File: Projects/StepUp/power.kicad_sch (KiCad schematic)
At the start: 28 parts, among them J2 USB_B_Micro, U2 NCP1117-3.3_SOT223, U3 MIC2253, U7 MCP73832T-2ACI_OT, U8 USBLC6-2SC6

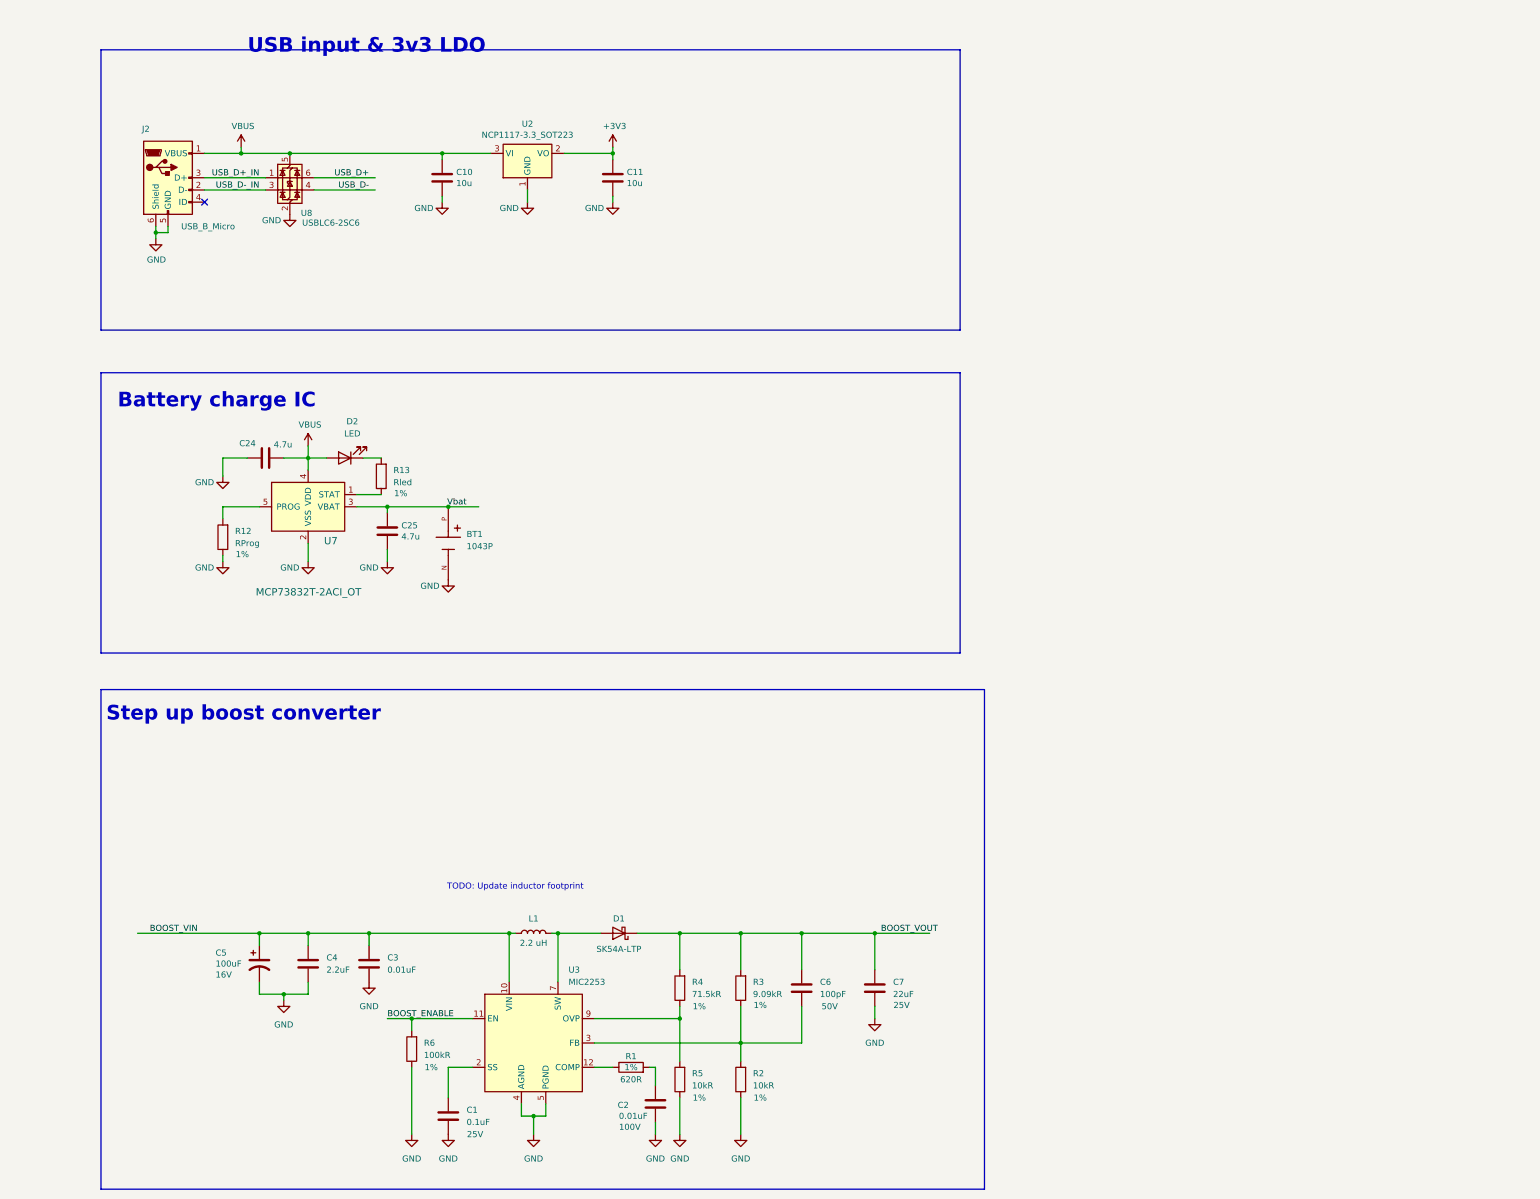
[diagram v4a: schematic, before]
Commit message: feat(power): Input stage updates
USB vs Vbat source selection using PMOS gate logic.
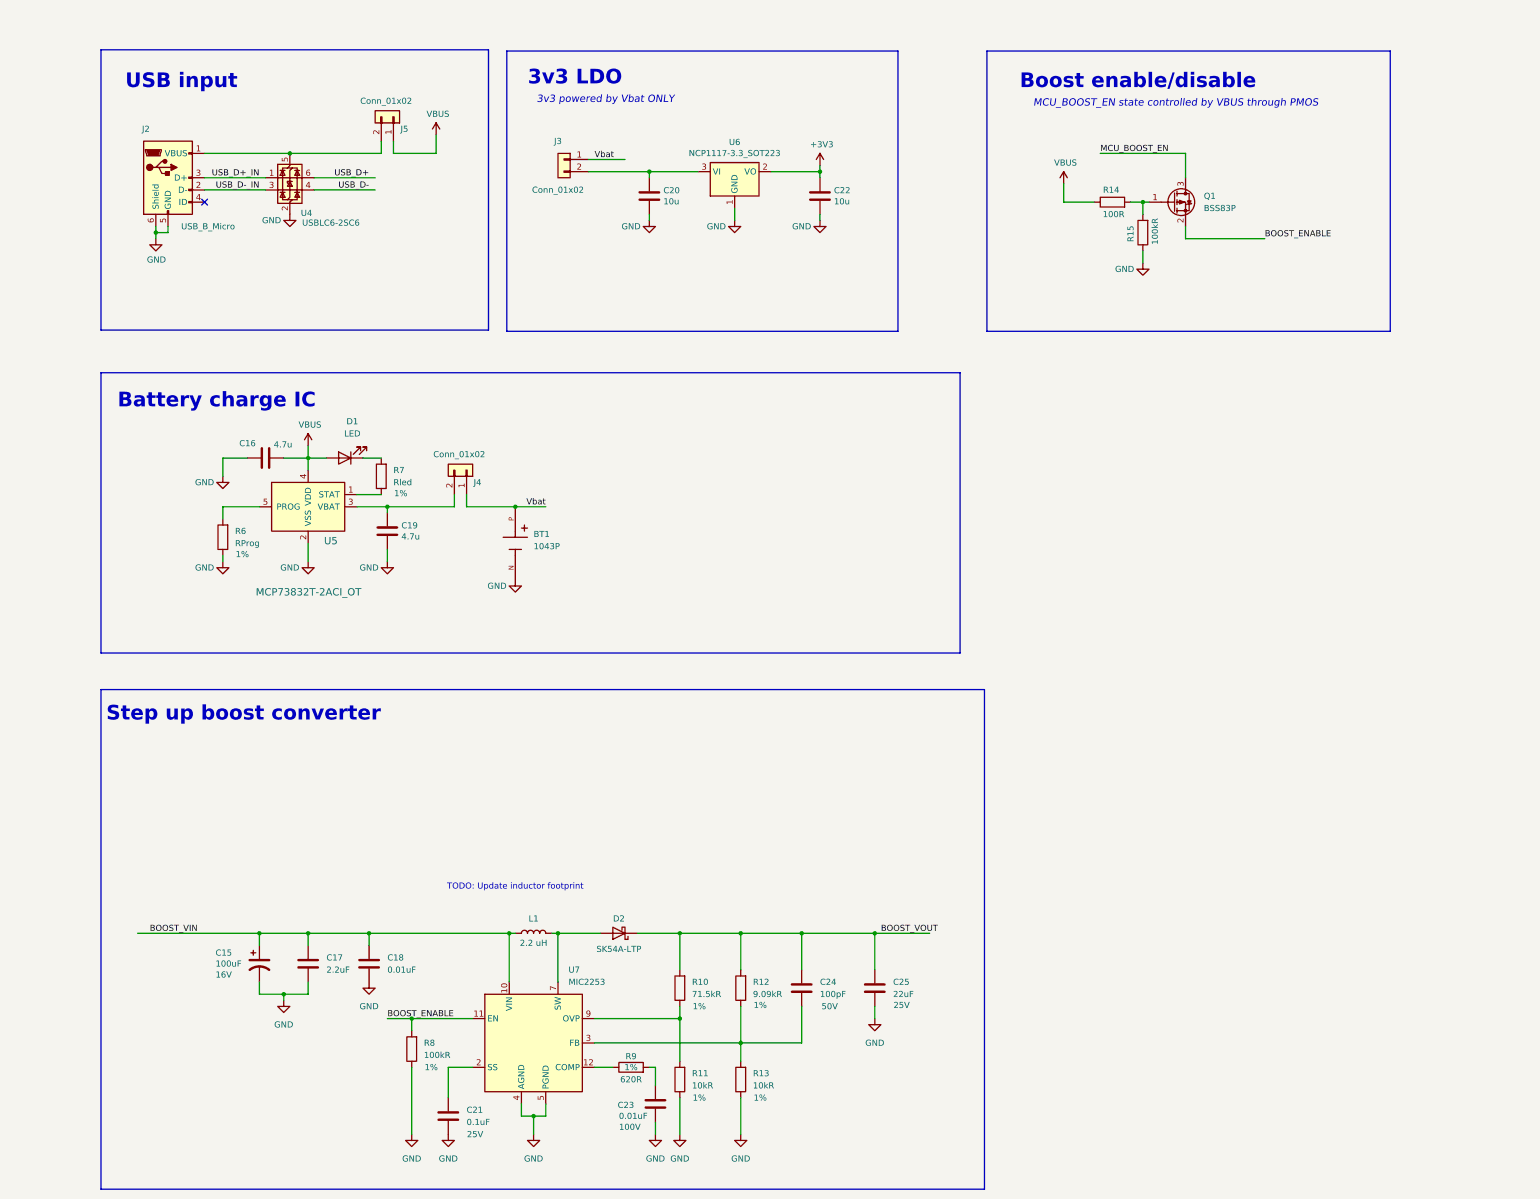
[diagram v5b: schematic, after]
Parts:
- added J3, J4, J5: Conn_01x02, Connector_PinHeader_2.54mm:PinHeader_1x02_P2.54mm_Vertical, symbol Connector_Generic:Conn_01x02
- added Q1: BSS83P, Package_TO_SOT_SMD:SOT-23, symbol Transistor_FET:BSS83P
- added R14: 100R, Resistor_SMD:R_0603_1608Metric, symbol Device:R
- added R15: 100kR, Resistor_SMD:R_0603_1608Metric, symbol Device:R
- renumbered C5 to C15, C24 to C16, C4 to C17, C3 to C18, C25 to C19, C10 to C20, C1 to C21, C11 to C22, C2 to C23, C6 to C24, C7 to C25, D2 to D1, D1 to D2, R4 to R10, R5 to R11, R3 to R12, R2 to R13, R12 to R6, R13 to R7, R6 to R8, R1 to R9, U8 to U4, U7 to U5, U2 to U6, U3 to U7
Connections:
- net BOOST_ENABLE: now also Q1.2 (S)
- net GND: now also R15.1
- net VBUS: now also J5.1 (Pin_1), R14.1; no longer C20.1, J2.1 (VBUS), U4.5 (VBUS), U6.3 (VI)
- net Vbat: now also J3.1 (Pin_1), J4.1 (Pin_1); no longer C19.1, U5.3 (VBAT)
- new net: Q1.1 (G), R14.2, R15.2
- new net: J2.1 (VBUS), J5.2 (Pin_2), U4.5 (VBUS)
- new net: C19.1, J4.2 (Pin_2), U5.3 (VBAT)
- new net: C20.1, J3.2 (Pin_2), U6.3 (VI)
- new net MCU_BOOST_EN: Q1.3 (D)
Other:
- note added: "3v3 LDO"
- note added: "3v3 powered by Vbat ONLY"
- note added: "Boost enable/disable"
- note added: "MCU_BOOST_EN state controlled by VBUS through PMOS"
- note added: "USB input"
- note removed: "USB input & 3v3 LDO"
- moved on the sheet: BT1, C20, C22, U6

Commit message: feat(stepup): Many additions
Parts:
- removed J2: USB_B_Micro, Connector_USB:USB_Micro-B_Amphenol_10103594-0001LF_Horizontal, symbol Connector:USB_B_Micro
- removed J3: Conn_01x02, Connector_PinHeader_2.54mm:PinHeader_1x02_P2.54mm_Vertical, symbol Connector_Generic:Conn_01x02
- added C27, C30: 0.1uF, Capacitor_SMD:C_0603_1608Metric, symbol Device:C
- added D3: PMEG2020EH, Diode_SMD:D_SOD-123F, symbol Diode:PMEG2020EH
- added J1, J7: Conn_01x02, Connector_PinHeader_2.54mm:PinHeader_1x02_P2.54mm_Vertical, symbol Connector_Generic:Conn_01x02
- added J8: USB_C_Receptacle_USB2.0_16P, Connector_USB:USB_C_Receptacle_GCT_USB4105-xx-A_16P_TopMnt_Horizontal, symbol Connector:USB_C_Receptacle_USB2.0_16P
- added JP1: SolderJumper_2_Open, Jumper:SolderJumper-2_P1.3mm_Open_RoundedPad1.0x1.5mm, symbol Jumper:SolderJumper_2_Open
- added Q2: BSS83P, Package_TO_SOT_SMD:SOT-23, symbol Transistor_FET:BSS83P
- added R16, R17: 5.1kR, Resistor_SMD:R_0603_1608Metric, symbol Device:R
- added R18: 10kR, Resistor_SMD:R_0603_1608Metric, symbol Device:R
- added R19, R20, R21, R22: 100kR, Resistor_SMD:R_0603_1608Metric, symbol Device:R
- added TP1: TestPoint, symbol Connector:TestPoint
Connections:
- net BOOST_ENABLE: now also JP1.1 (A)
- net BOOST_VIN: now also J7.2 (Pin_2)
- net BOOST_VOUT: now also TP1.1
- net GND: now also C27.1, C30.1, J8.A1 (GND), J8.A12 (GND), J8.B1 (GND), J8.B12 (GND), J8.S1 (SHIELD), R16.1, R17.1, R18.2, R19.1, R22.1
- net MCU_BOOST_EN: now also JP1.2 (B)
- net USB_D+_IN: now also J8.A6 (D+), J8.B6 (D+)
- net USB_D-_IN: now also J8.A7 (D-), J8.B7 (D-)
- net Vbat: now also J7.1 (Pin_1), Q2.3 (D), R20.2
- net at J5.2 (Pin_2), U4.5 (VBUS): now also J8.A4 (VBUS), J8.A9 (VBUS), J8.B4 (VBUS), J8.B9 (VBUS)
- net at C20.1, U6.3 (VI): now also D3.1 (K), Q2.2 (S)
- net VBUS renamed V_USB
- net V_USB: now also J1.1 (Pin_1), R21.2
- new net: D3.2 (A), J1.2 (Pin_2), Q2.1 (G), R18.1
- new net: J8.A5 (CC1), R16.2
- new net: J8.B5 (CC2), R17.2
- new net VUSB_monitor: C30.2, R21.1, R22.2
- new net Vbat_monitor: C27.2, R19.2, R20.1
- no-connect marks 1 -> 2
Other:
- note added: "3.3->4.2V VBat -> 1.65->2.6V ADC in"
- note added: "5V -> 2.5V - allow ability to detect this with digital pin on MCU"
- note added: "Includes decision logic for VBus vs VBat power"
- note added: "Voltage monitoring"
- note removed: "3v3 powered by Vbat ONLY"
- moved on the sheet: BT1, C15, C16, C17, C18, C19, C20, C21, C22, C23, C24, C25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

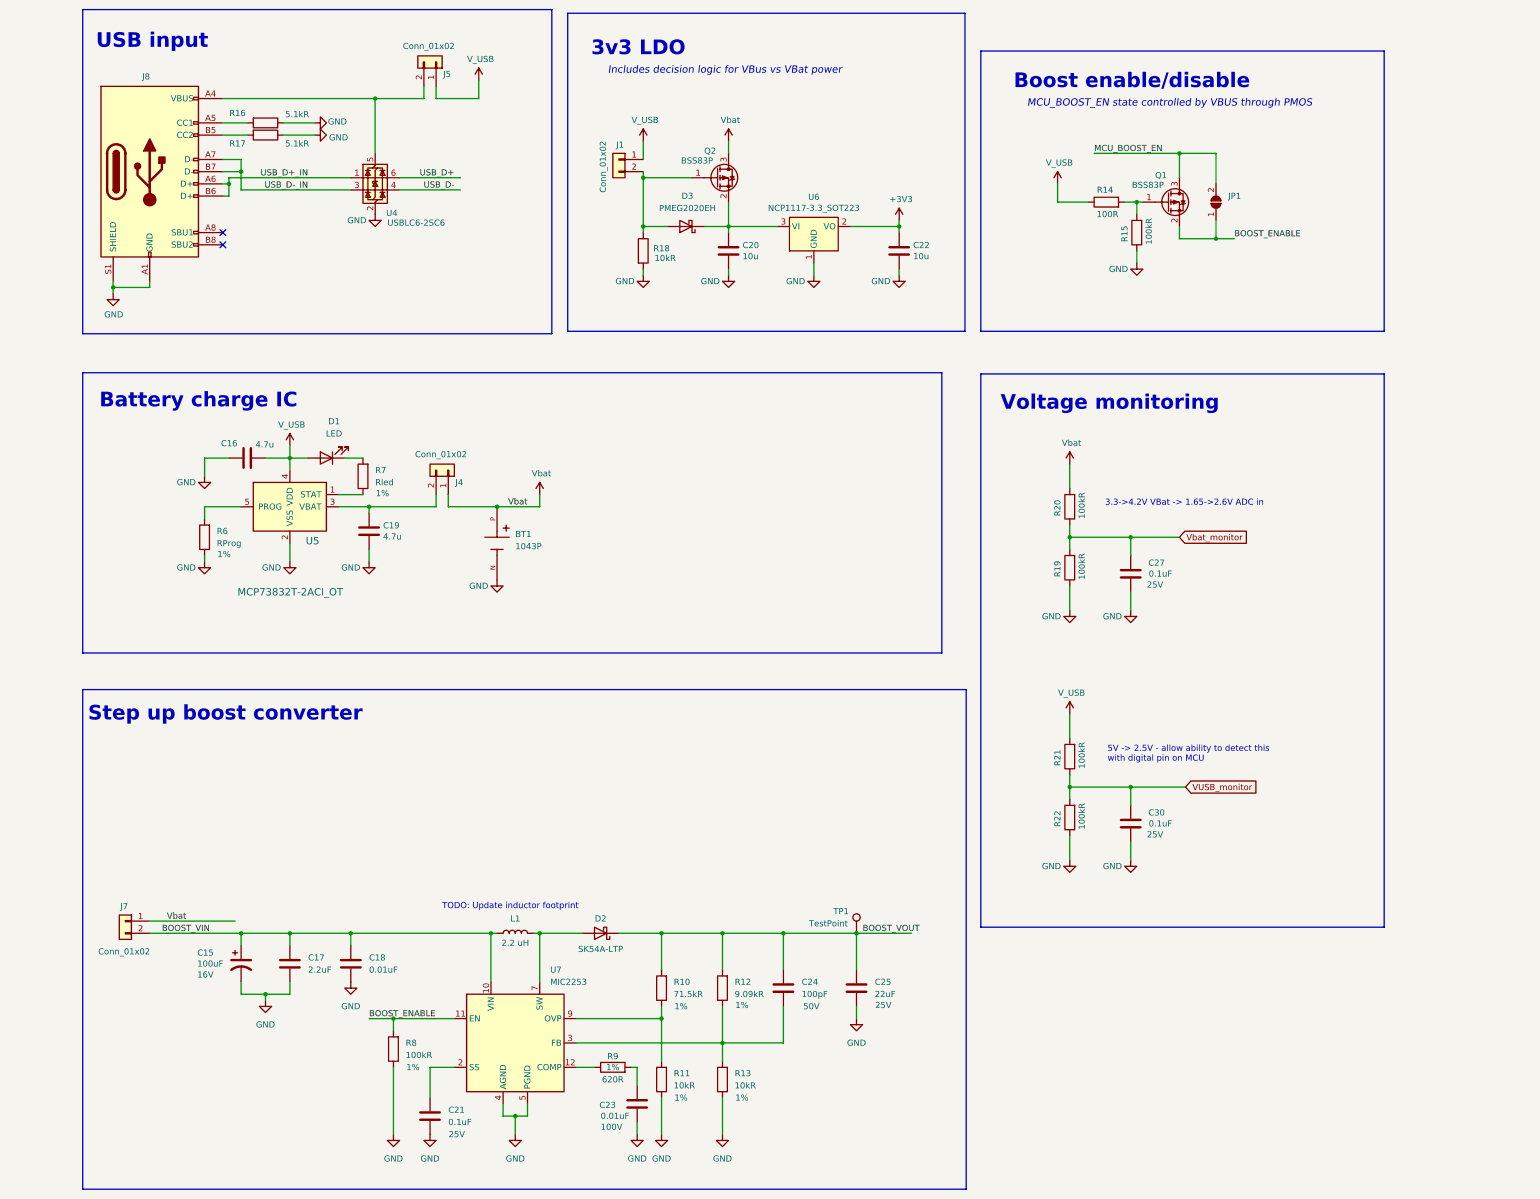
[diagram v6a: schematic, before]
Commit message: feat(stepup): Schematic + PCB updates
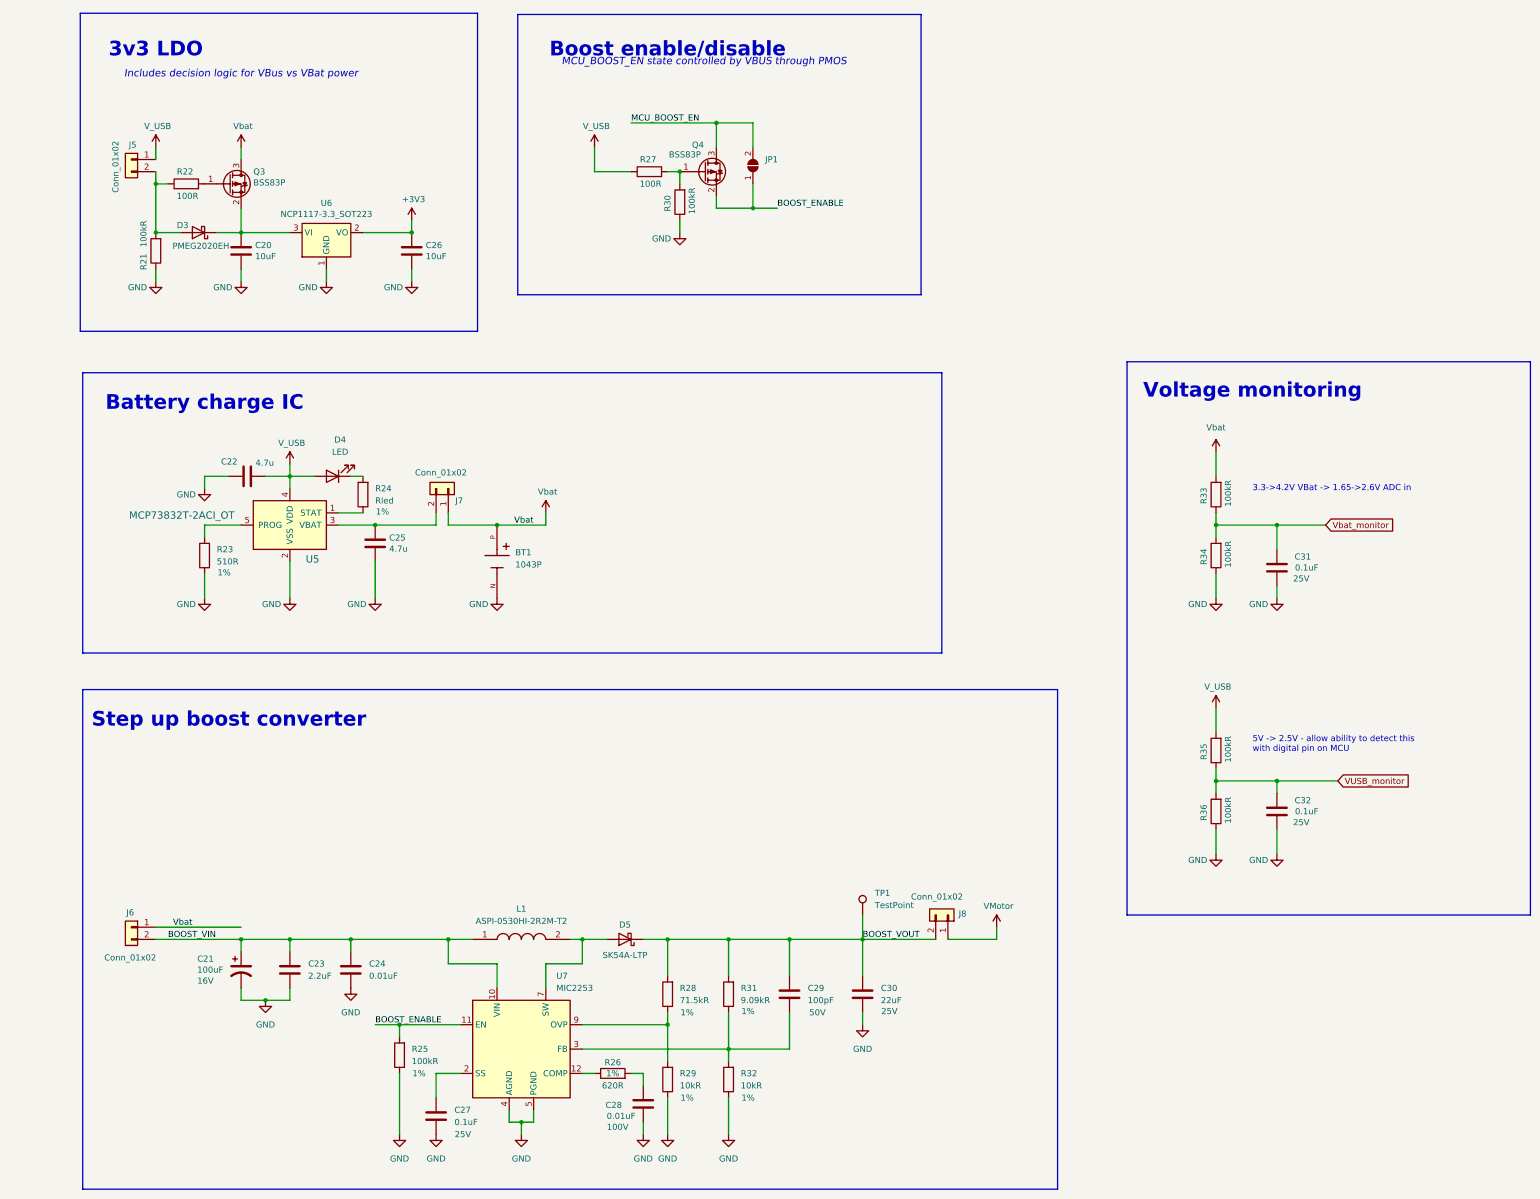
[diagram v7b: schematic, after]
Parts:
- removed J5: Conn_01x02, Connector_PinHeader_2.54mm:PinHeader_1x02_P2.54mm_Vertical, symbol Connector_Generic:Conn_01x02
- removed J8: USB_C_Receptacle_USB2.0_16P, Connector_USB:USB_C_Receptacle_GCT_USB4105-xx-A_16P_TopMnt_Horizontal, symbol Connector:USB_C_Receptacle_USB2.0_16P
- removed L1: 2.2 uH, Inductor_SMD:L_Abracon_ASPI-4030S, symbol Device:L
- removed R16, R17: 5.1kR, Resistor_SMD:R_0603_1608Metric, symbol Device:R
- removed R18: 10kR, Resistor_SMD:R_0603_1608Metric, symbol Device:R
- removed U4: USBLC6-2SC6, Package_TO_SOT_SMD:SOT-23-6, symbol Power_Protection:USBLC6-2SC6
- added J8: Conn_01x02, Connector_PinHeader_2.54mm:PinHeader_1x02_P2.54mm_Vertical, symbol Connector_Generic:Conn_01x02
- added L1: ASPI-0530HI-2R2M-T2, Samacsys:INDPM5652X300N, symbol Samacsys:ASPI-0530HI-2R2M-T2
- added R21: 100kR, Resistor_SMD:R_0603_1608Metric, symbol Device:R
- added R22: 100R, Resistor_SMD:R_0603_1608Metric, symbol Device:R
- C20: value 10u -> 10uF
- C26: renamed from C22; value 10u -> 10uF
- R23: renamed from R6; value RProg -> 510R
- TP1: footprint (none) -> TestPoint:TestPoint_Pad_D1.5mm
- renumbered C15 to C21, C16 to C22, C17 to C23, C18 to C24, C19 to C25, C21 to C27, C23 to C28, C24 to C29, C25 to C30, C27 to C31, C30 to C32, D1 to D4, D2 to D5, J1 to J5, J7 to J6, J4 to J7, Q2 to Q3, Q1 to Q4, R7 to R24, R8 to R25, R9 to R26, R14 to R27, R10 to R28, R11 to R29, R15 to R30, R12 to R31, R13 to R32, R20 to R33, R19 to R34, R21 to R35, R22 to R36
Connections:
- net BOOST_VIN: now also L1.1
- net BOOST_VOUT: now also J8.2 (Pin_2)
- net GND: now also R21.1
- net at D5.2 (A), U7.7 (SW), U7.8 (SW): now also L1.2
- net at D3.2 (A), J5.2 (Pin_2): now also R21.2, R22.1; no longer Q3.1 (G)
- new net: Q3.1 (G), R22.2
- new net VMotor: J8.1 (Pin_1)
- no-connect marks 2 -> 0
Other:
- note removed: "TODO: Update inductor footprint"
- note removed: "USB input"
- moved on the sheet: BT1, C20, C21, C22, C23, C24, C25, C26, C27, C28, C29, C30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
